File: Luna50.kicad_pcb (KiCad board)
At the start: 2 copper layers, 276.2 x 87.2 mm, 112 parts, among them J1 USB_B_Mini, SW0 SW_Push, SW1 Esc, SW10 O, SW11 P, SW12 [, SW13 ], SW14 Bsp, SW15 Tab_125, SW16 A, SW17 S, SW18 D, SW19 F, SW2 Q, SW20 G, SW21 H, SW22 J, SW23 K, SW24 L, SW25 ;, SW26 ', SW27 Ent_175, SW28 LShft_175, SW29 Z, SW3 W, SW30 X, SW31 C, SW32 V, SW33 B, SW34 N, SW35 M, SW36 ,, SW37 ., SW38 /, SW39 RShft_225, SW4 E, SW40 LCtrl_125, SW41 Win_125, SW42 LAlt_125, SW43 Space_625, SW44 RAlt_125, SW45 Fn_125, SW46 RCtrl_150, SW5 R, SW6 T, SW7 Y, SW8 U, SW9 I, U1 ATmega32U4-AU, Y1 16MHz

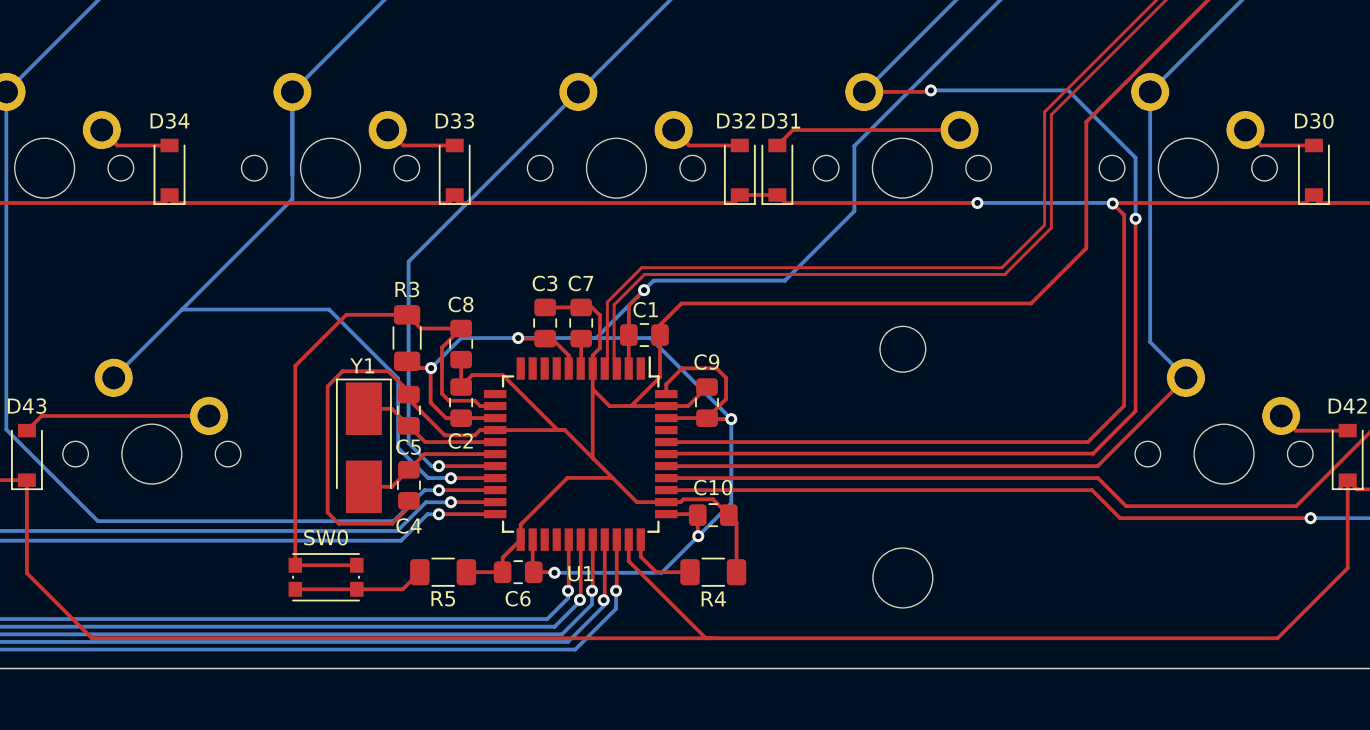
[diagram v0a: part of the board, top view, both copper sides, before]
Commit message: Update Paths
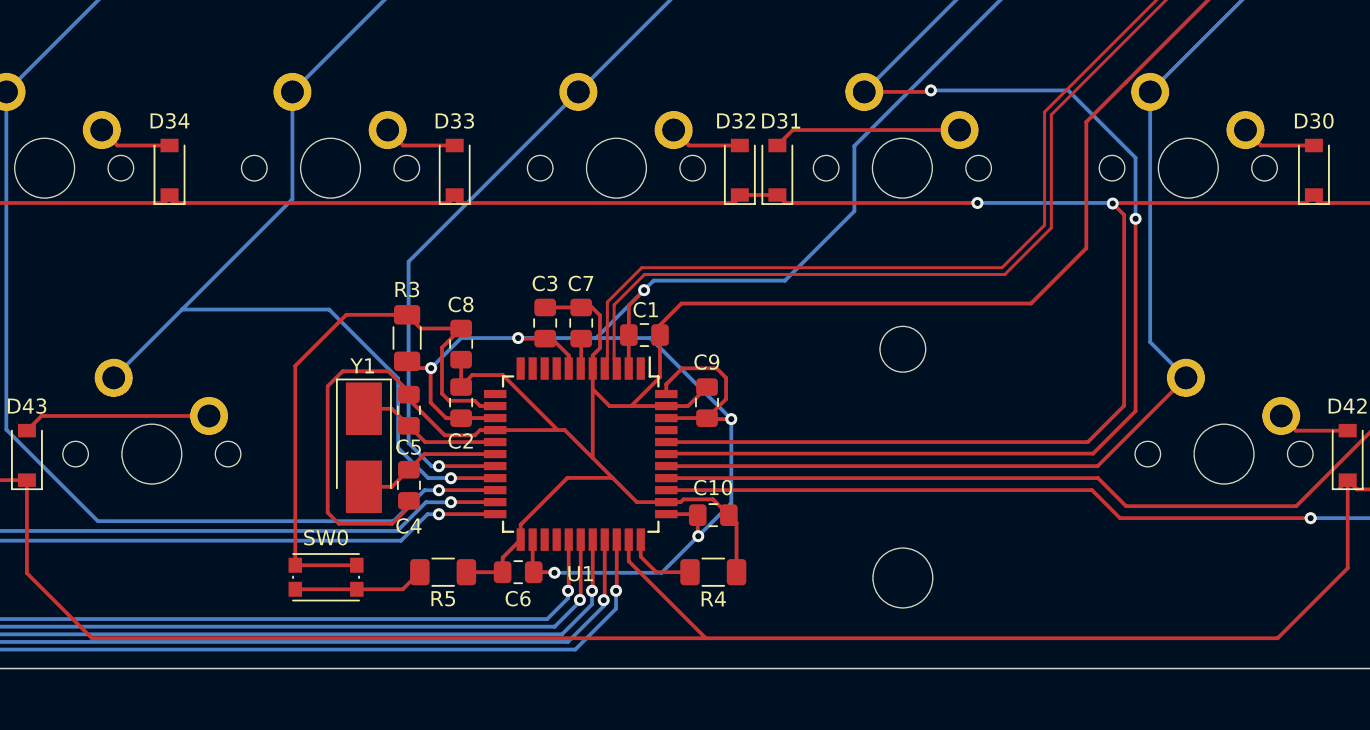
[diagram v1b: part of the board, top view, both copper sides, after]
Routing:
- net Col6: track 101.8 -> 96.2 mm
- net Col4: track 107.0 -> 105.8 mm
- net GND: track 194.7 -> 193.9 mm
